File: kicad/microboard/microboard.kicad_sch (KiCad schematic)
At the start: 5 parts, among them J1 Conn_01x04_Socket, U1 TMP235A4DCKR, U2 DRV5011ADDBZR

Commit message: kicad: pcb v0.99
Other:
- note added: "2.3-5.5V, 9µA, max out 30mA@VDD±0.3 (0.159W), operational to 150C."
- note added: "2.5-5.5V, 3mA, max out 30mA@VDD±0.3 (0.159W), operational to 135C."
- note removed: "2.3-5.5V, 9µA, max out 30mA@VDD±0.3 (0.159W), op to 150C."
- note removed: "2.5-5.5V, 3mA, max out 30mA@VDD±0.3 (0.159W), op to 135C."
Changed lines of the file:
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@@
 		)
 	)
-	(text "2.5-5.5V, 3mA, max out 30mA@VDD±0.3 (0.159W),\n op to 135C."
+	(text "2.5-5.5V, 3mA, max out 30mA@VDD±0.3 (0.159W),\n operational to 135C."
 		(exclude_from_sim no)
 		(at 71.882 101.092 0)
@@
 		)
 	)
-	(text "2.3-5.5V, 9µA, max out 30mA@VDD±0.3 (0.159W),\n op to 150C."
+	(text "2.3-5.5V, 9µA, max out 30mA@VDD±0.3 (0.159W),\n operational to 150C."
 		(exclude_from_sim no)
 		(at 135.128 100.838 0)

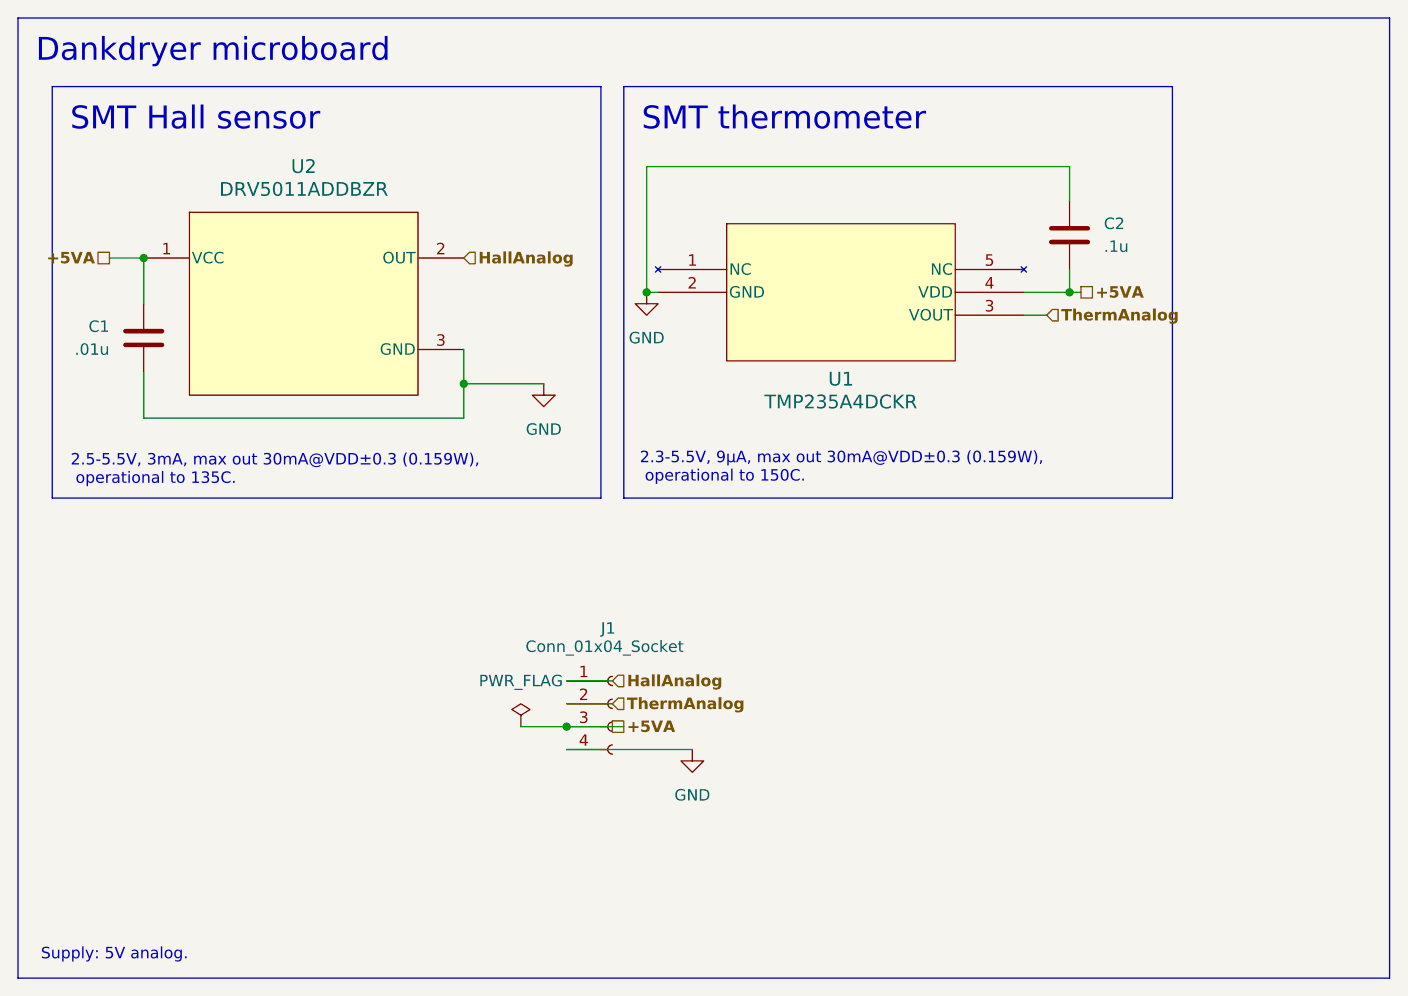
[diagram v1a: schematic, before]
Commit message: update microboard for current 5-pin connector
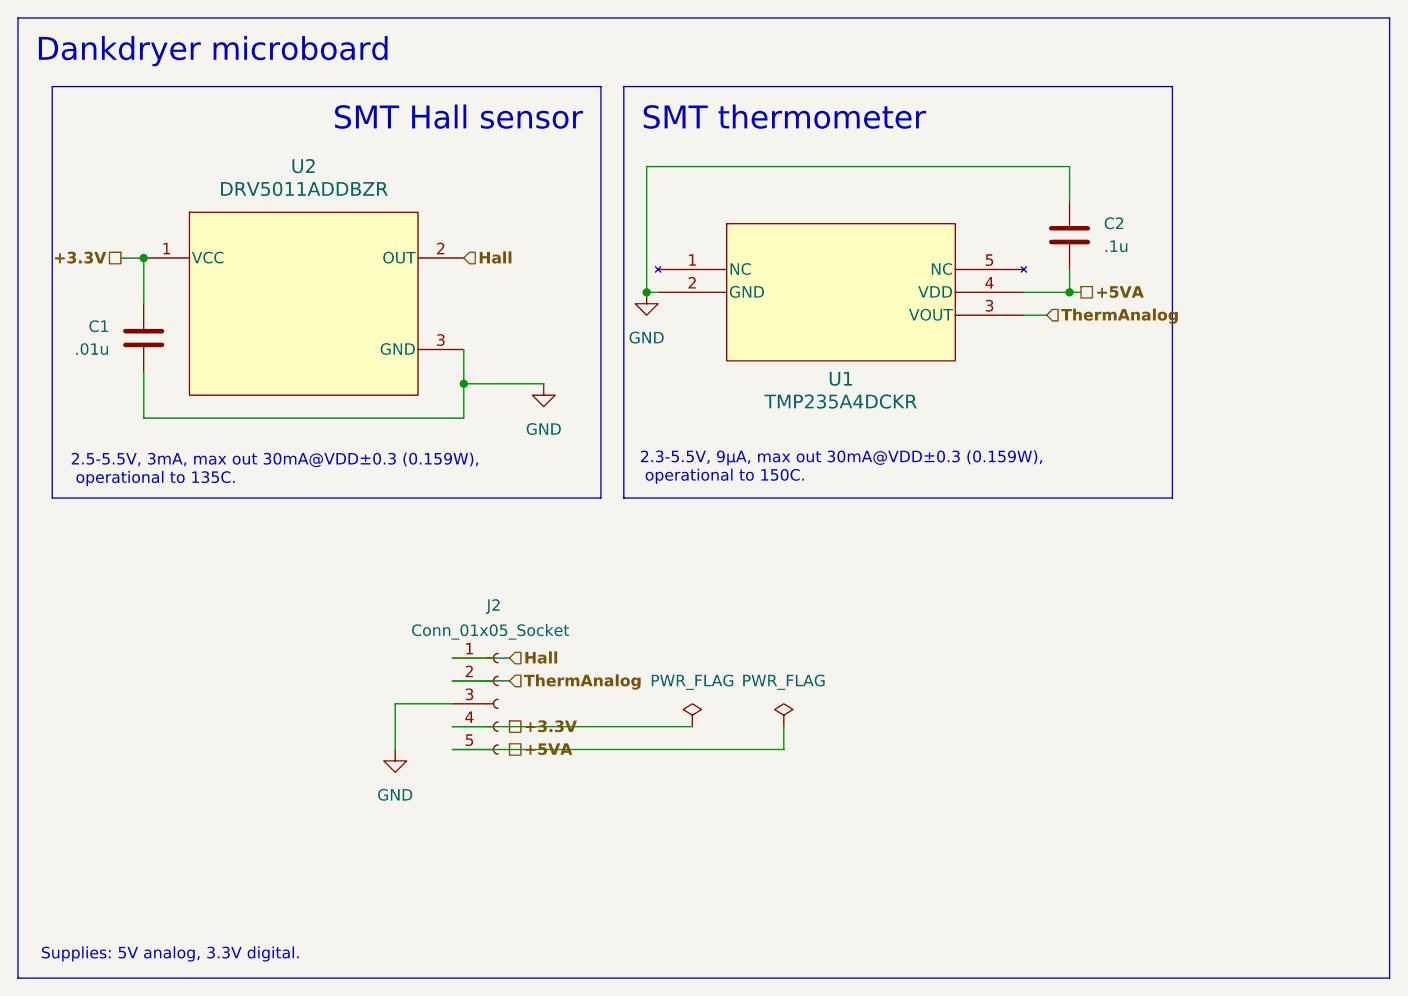
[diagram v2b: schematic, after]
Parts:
- removed J1: Conn_01x04_Socket, Connector_PinSocket_1.00mm:PinSocket_1x04_P1.00mm_Vertical, symbol Connector:Conn_01x04_Socket
- added J2: Conn_01x05_Socket, Connector_PinSocket_1.00mm:PinSocket_1x05_P1.00mm_Vertical, symbol Connector:Conn_01x05_Socket
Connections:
- net +5VA: now also J2.5 (Pin_5); no longer C1.1, U2.1 (VCC)
- net GND: now also J2.3 (Pin_3)
- net ThermAnalog: now also J2.2 (Pin_2)
- net HallAnalog renamed Hall
- net Hall: now also J2.1 (Pin_1)
- new net +3.3V: C1.1, J2.4 (Pin_4), U2.1 (VCC)
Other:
- note added: "Supplies: 5V analog, 3.3V digital."
- note removed: "Supply: 5V analog."

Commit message: beefier capacitors on the microboard
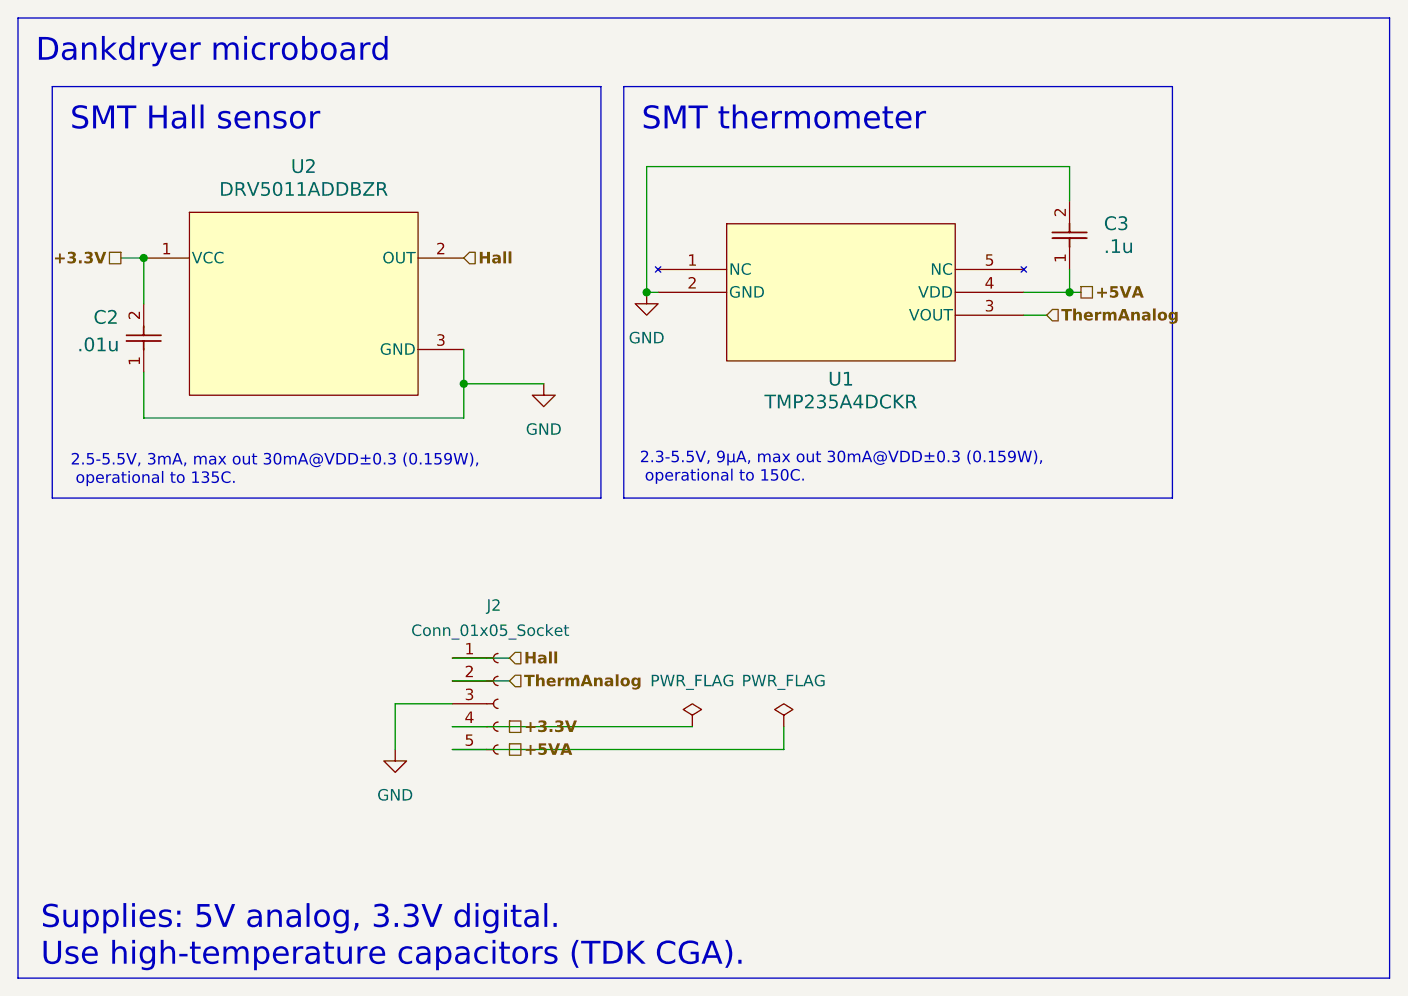
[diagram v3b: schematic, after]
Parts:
- removed C1: .01u, Capacitor_SMD:C_0805_2012Metric_Pad1.18x1.45mm_HandSolder, symbol Device:C
- removed C2: .1u, Capacitor_SMD:C_0805_2012Metric_Pad1.18x1.45mm_HandSolder, symbol Device:C
- added C2: .01u, dank:CAP_3216_TDK, symbol dank:CGA5L2NP01H104J160AA
- added C3: .1u, dank:CAP_3216_TDK, symbol dank:CGA5L2NP01H104J160AA
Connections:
- net +3.3V: now also C2.2
- net +5VA: now also C3.1
- net GND: now also C2.1, C3.2
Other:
- note added: "Supplies: 5V analog, 3.3V digital. Use high-temperature capacitors (TDK CGA)."
- note removed: "Supplies: 5V analog, 3.3V digital."
- company: Dirty South Supercomputing -> dirty south supercomputing
- title: Dankdryer microboard -> dankdryer microboard
